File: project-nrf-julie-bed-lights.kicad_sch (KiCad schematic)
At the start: 22 parts

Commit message: Annotate
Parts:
- gave numbers to parts that had none: 22

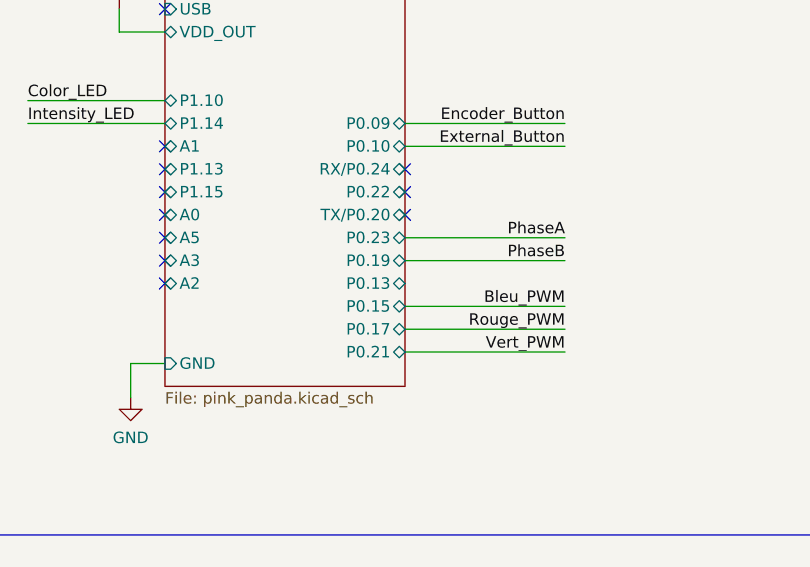
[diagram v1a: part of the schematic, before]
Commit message: Fix schematic errors
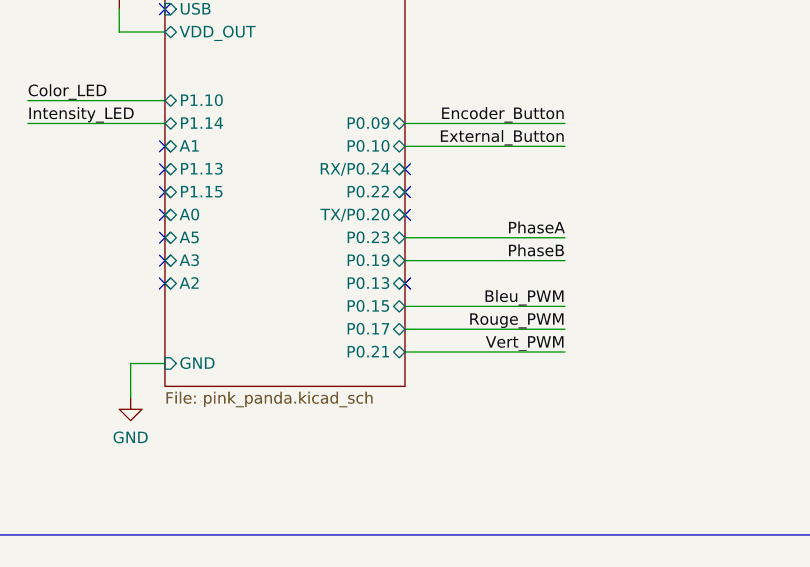
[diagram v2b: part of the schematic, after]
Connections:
- no-connect marks 12 -> 13

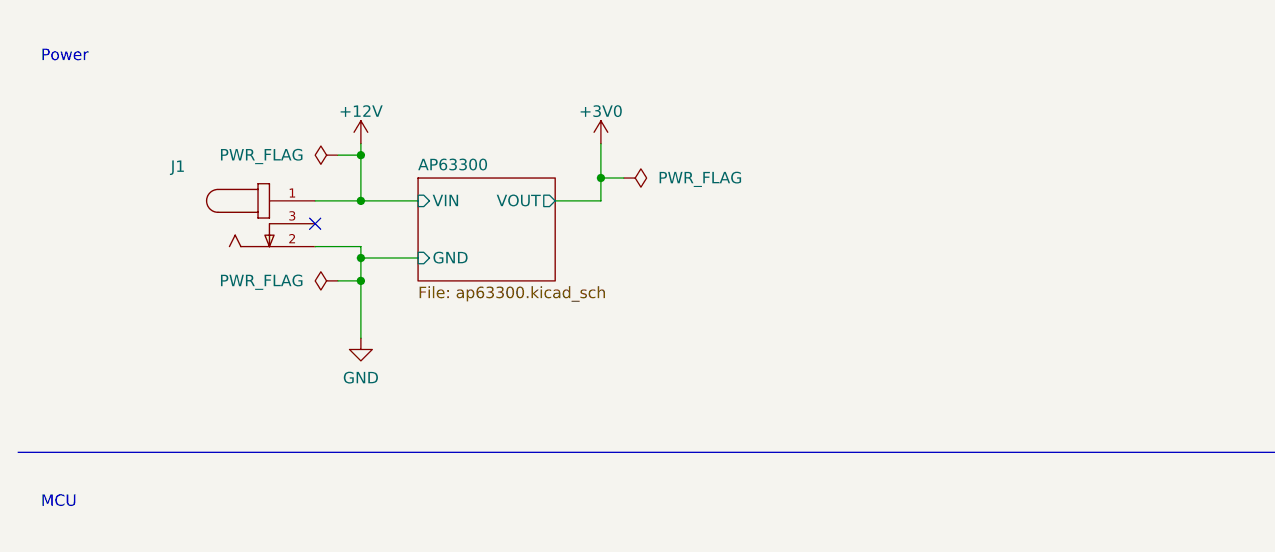
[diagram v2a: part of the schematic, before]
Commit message: Add input protection
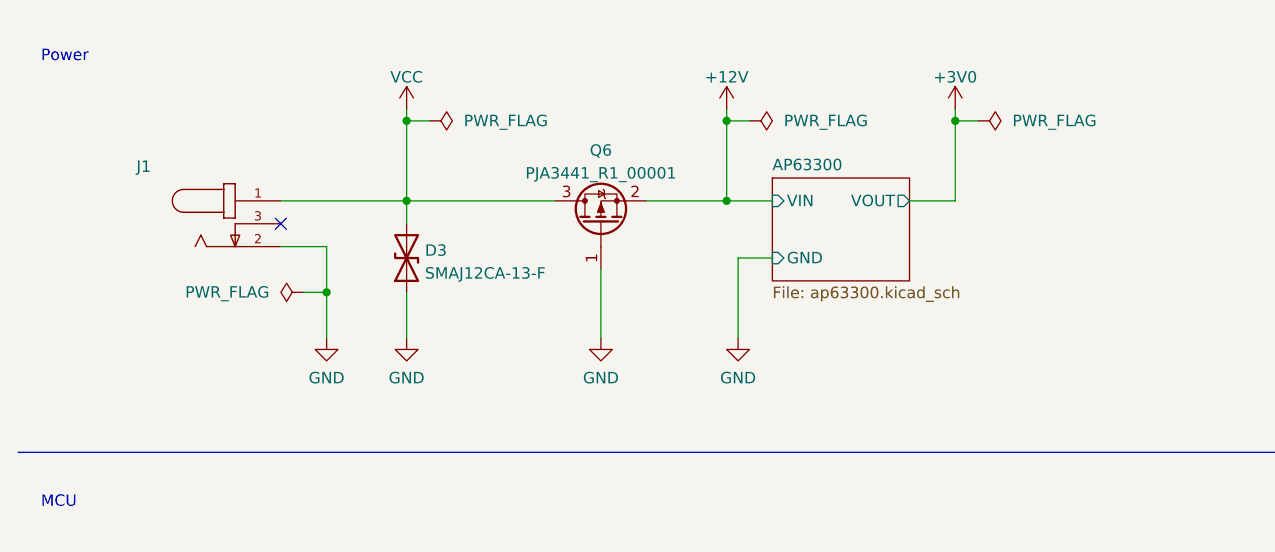
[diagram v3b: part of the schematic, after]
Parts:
- added D3: SMAJ12CA-13-F, Diode_SMD:D_SMA, symbol Device:D_TVS
- added Q6: PJA3441_R1_00001, Package_TO_SOT_SMD:SOT-23, symbol Device:Q_PMOS_GSD
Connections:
- net +12V: now also Q6.2 (S); no longer J1.1
- net GND: now also D3.1 (A1), Q6.1 (G)
- new net VCC: D3.2 (A2), J1.1, Q6.3 (D)
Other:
- moved on the sheet: J1

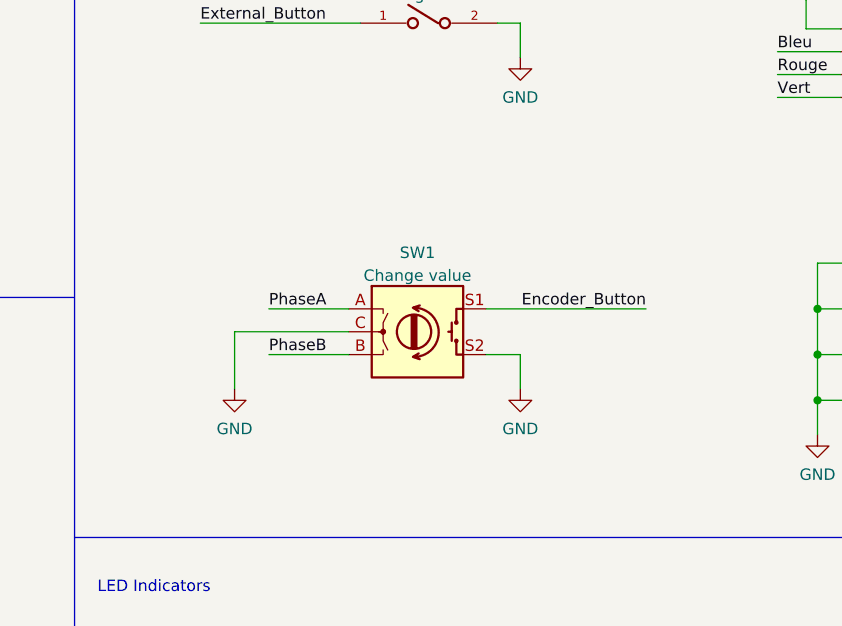
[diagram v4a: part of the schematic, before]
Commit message: Add pull-ups to the rotary encoder
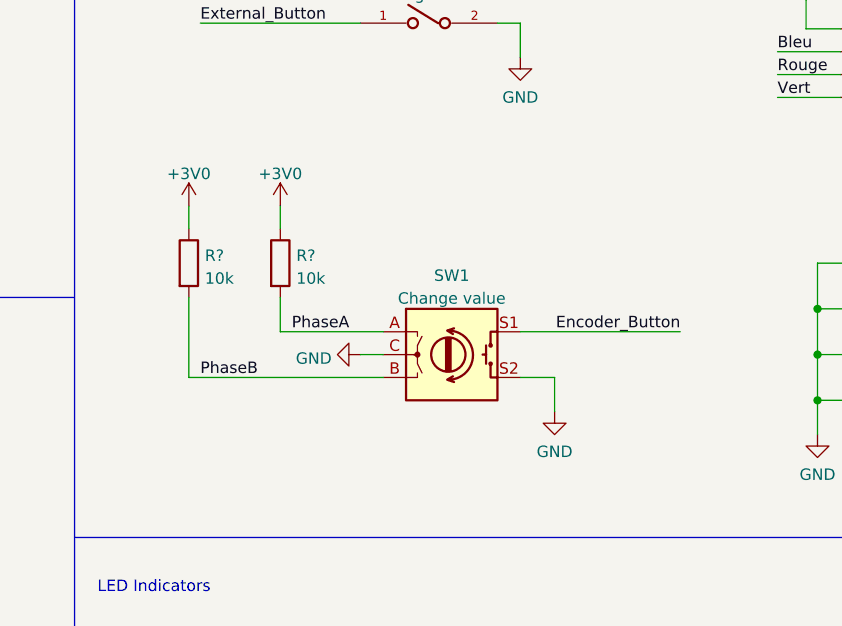
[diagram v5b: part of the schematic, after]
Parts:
- added R? (x2): 10k, Resistor_SMD:R_0603_1608Metric, symbol Device:R
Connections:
- net +3V0: now also R?.1, R?.1
- net PhaseA: now also R?.2
- net PhaseB: now also R?.2
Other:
- moved on the sheet: SW1

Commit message: Update board
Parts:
- gave numbers to parts that had none: 2
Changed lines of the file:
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@@
   (symbol (lib_id "Device:R") (at 199.39 57.15 0) (unit 1)
     (in_bom yes) (on_board yes) (fields_autoplaced)
-    (property "Reference" "R?" (id 0) (at 201.168 56.3153 0)
+    (property "Reference" "R11" (id 0) (at 201.168 56.3153 0)
       (effects (font (size 1.27 1.27)) (justify left))
     )
@@
   (symbol (lib_id "power:+3V0") (at 189.23 50.8 0) (unit 1)
     (in_bom yes) (on_board yes)
-    (property "Reference" "#PWR?" (id 0) (at 189.23 54.61 0)
+    (property "Reference" "#PWR0104" (id 0) (at 189.23 54.61 0)
       (effects (font (size 1.27 1.27)) hide)
     )
@@
   (symbol (lib_id "power:+3V0") (at 199.39 50.8 0) (unit 1)
     (in_bom yes) (on_board yes)
-    (property "Reference" "#PWR?" (id 0) (at 199.39 54.61 0)
+    (property "Reference" "#PWR0105" (id 0) (at 199.39 54.61 0)
       (effects (font (size 1.27 1.27)) hide)
     )
@@
   (symbol (lib_id "Device:R") (at 189.23 57.15 0) (unit 1)
     (in_bom yes) (on_board yes) (fields_autoplaced)
-    (property "Reference" "R?" (id 0) (at 191.008 56.3153 0)
+    (property "Reference" "R10" (id 0) (at 191.008 56.3153 0)
       (effects (font (size 1.27 1.27)) (justify left))
     )
@@
       (reference "#PWR0103") (unit 1) (value "+3V0") (footprint "")
     )
+    (path "/72c1280e-8fec-49ae-a5f7-80661351f2fa"
+      (reference "#PWR0104") (unit 1) (value "+3V0") (footprint "")
+    )
+    (path "/833f1f54-7666-4eee-bf8b-f1a2b51aa75d"
+      (reference "#PWR0105") (unit 1) (value "+3V0") (footprint "")
+    )
     (path "/4401e248-82ba-4657-bdfc-f2c247204611"
       (reference "#PWR0106") (unit 1) (value "GND") (footprint "")
@@
       (reference "#PWR0126") (unit 1) (value "GND") (footprint "")
     )
-    (path "/72c1280e-8fec-49ae-a5f7-80661351f2fa"
-      (reference "#PWR?") (unit 1) (value "+3V0") (footprint "")
-    )
-    (path "/833f1f54-7666-4eee-bf8b-f1a2b51aa75d"
-      (reference "#PWR?") (unit 1) (value "+3V0") (footprint "")
-    )
     (path "/518ff29c-c2ce-424a-acd0-9cec8c6e8c30/7b397fc9-9134-481c-8494-648dd634e85f"
       (reference "C1") (unit 1) (value "10uF") (footprint "Capacitor_SMD:C_0805_2012Metric")
@@
       (reference "R9") (unit 1) (value "1k") (footprint "Resistor_SMD:R_0603_1608Metric")
     )
+    (path "/ad764fde-1da9-4b57-ae8a-331b47e15433"
+      (reference "R10") (unit 1) (value "10k") (footprint "Resistor_SMD:R_0603_1608Metric")
+    )
     (path "/5cf31990-bfab-4dea-989e-b52dbb55aa53"
-      (reference "R?") (unit 1) (value "10k") (footprint "Resistor_SMD:R_0603_1608Metric")
-    )
-    (path "/ad764fde-1da9-4b57-ae8a-331b47e15433"
-      (reference "R?") (unit 1) (value "10k") (footprint "Resistor_SMD:R_0603_1608Metric")
+      (reference "R11") (unit 1) (value "10k") (footprint "Resistor_SMD:R_0603_1608Metric")
     )
     (path "/c03bf16d-2761-46d1-8101-d921680d07b3"
